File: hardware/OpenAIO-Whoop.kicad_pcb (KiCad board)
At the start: 6 copper layers, 30.3 x 30.3 mm, 248 parts, among them J1 U.FL, J10 M3, J13 M4, J2 +, J20 LED, J21 5V, J22 BZ-, J23 CAM, J24 5V, J25 GND, J26 VHD, J27 GND, J28 TX0, J29 RX0, J3 -, J31 USB, J32 CAM, J33 GND, J4 M1, J7 M2, Q26 AP1606, Q27 BC857BM, Q29 AGM210MAP, Q30 AGM210MAP, Q31 AGM210MAP, Q32 AGM210MAP, Q33 AGM210MAP, Q34 AGM210MAP, Q35 AGM210MAP, Q36 AGM210MAP, Q37 AGM210MAP, Q38 AGM210MAP, Q39 AGM210MAP, Q40 AGM210MAP, SW1 SKUBAAE010, U1 INA186A3, U10 RP2354A, U11 BMI270, U12 TPS7A2018, U13 PY25Q128HA-DFH-IR, U14 SN74LVC1G3157, U15 TLV7031, U16 ESP32-PICO-V3, U18 SX1281, U19 RTC6705, U2 TPS61022, U20 SE5004L, U21 LP5912-3.3, U22 TPS7A20285, U24 FXMAR2104UMX, U4 TLV75733, U6 EFM8BB51F16I, U7 EFM8BB51F16I, U8 EFM8BB51F16I, U9 EFM8BB51F16I, X1 12MHz, X3 52MHz TCXO, X4 8MHz 10pF

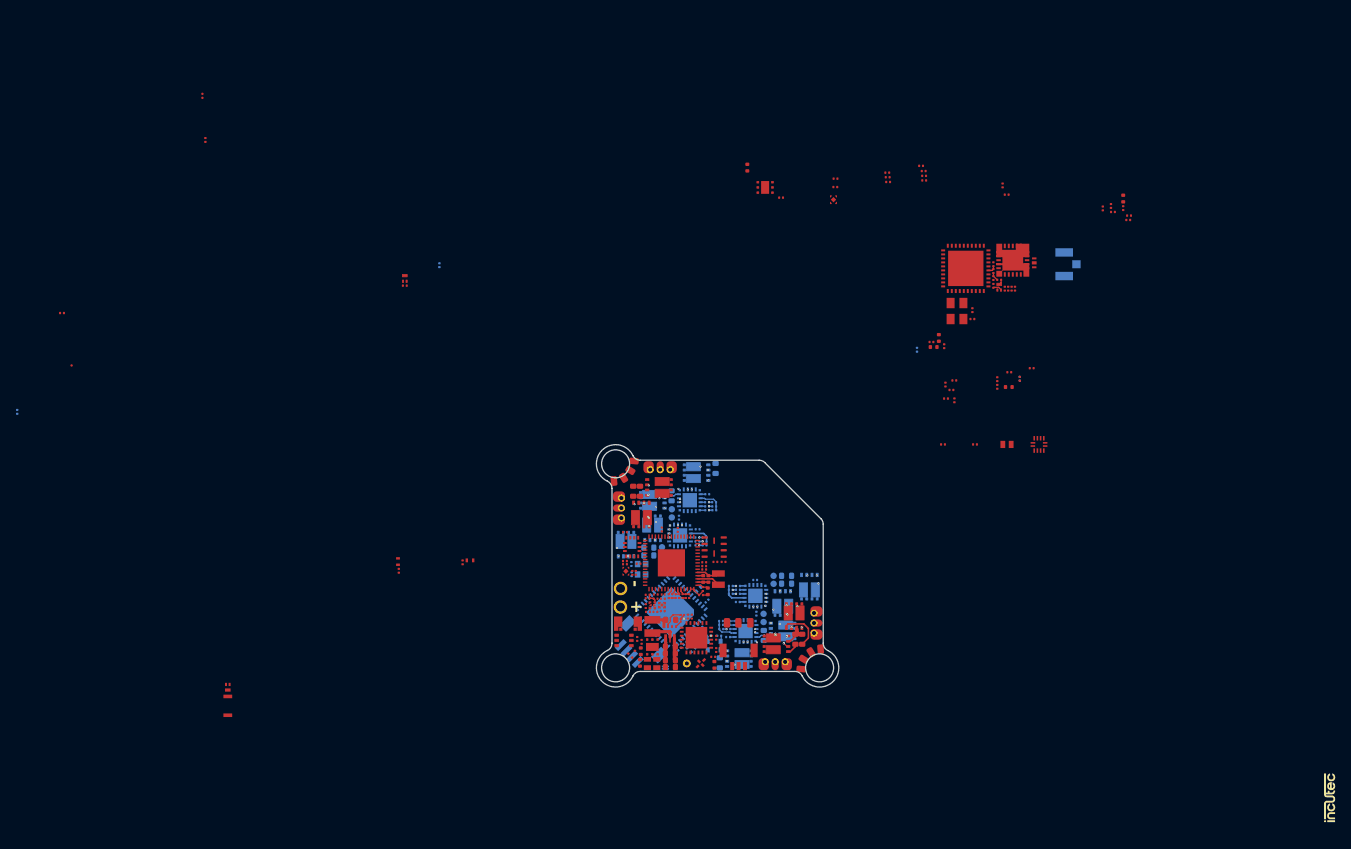
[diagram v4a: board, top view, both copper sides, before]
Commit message: Preserve owner ESC progress and allocate inner signal layers
Integrate the owner's retained placements and copper with the reviewed RP2354A mapping, restore both ESC bulk capacitors per channel, and carry the owner boot-testpoint deletion. Allocate In1/In4 for signals, In2 for continuous ground and In3 for power. Remove obsolete inner-layer routing restrictions and add native rule fixtures. This checkpoint precedes the new compact placement.

Validation: schematic parity zero; 28 GPIO mappings, 7 netlist checks and 32 rule fixtures pass. ERC has 12 existing warnings and no errors. The inherited board retains 269 DRC findings and 499 reported unconnected items. Layout is unfinished.
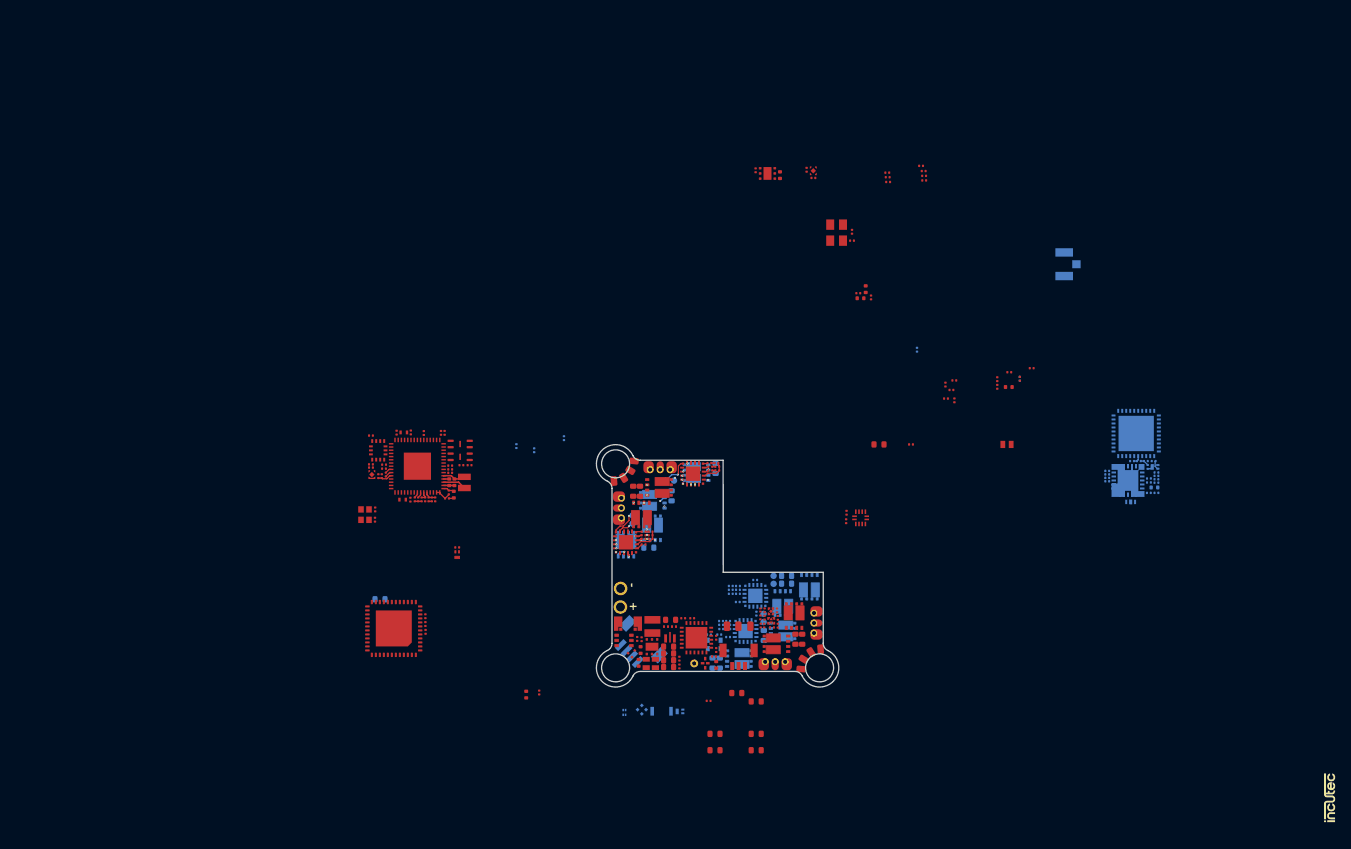
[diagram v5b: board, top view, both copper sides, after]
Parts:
- removed TP9: FCB, lib:TestPoint_Pad_D0.30mm_MicroVia_L
- added C22: 22uF, lib:C_0603_1608Metric_L, F.Cu at (118.0, 134.2)
- added C24: 22uF, lib:C_0603_1608Metric_L, F.Cu at (133.4, 98.0)
- added C28: 22uF, lib:C_0603_1608Metric_L, F.Cu at (112.9, 134.2)
- added C30: 22uF, lib:C_0603_1608Metric_L, F.Cu at (115.6, 129.1)
- added C34: 22uF, lib:C_0603_1608Metric_L, F.Cu at (118.0, 136.2)
- added C36: 22uF, lib:C_0603_1608Metric_L, B.Cu at (112.6, 125.3)
- added C40: 22uF, lib:C_0603_1608Metric_L, F.Cu at (112.9, 136.2)
- added C43: 22uF, lib:C_0603_1608Metric_L, F.Cu at (118.0, 130.2)
- C109, C110, C111, C112, C113, C114, C115, C116, C117, C118, C124, C125, D8, FL2, L3, Q27, R65, R66, R71, R72, R73, SW1, U19, U20: moved to B.Cu
- C42, C47, C70, C73, C76, C82, C83, C89, R26, R27, R28, R29, R30, R31, R32, R34, R35, R36, R37, R38, R39, R44, R56, U16, U8, U9, X1: moved to F.Cu
- moved C70 63.1 mm to (137.4, 98.0), turned to 0 degrees
- moved D8 56.6 mm to (108.5, 131.4), turned to 0 degrees
- moved SW1 54.2 mm to (106.2, 131.4), turned to 180 degrees
- moved R44 53.5 mm to (79.1, 96.6)
- moved TP13 53.0 mm to (71.7, 102.0), turned to 180 degrees
- moved TP12 52.2 mm to (71.7, 101.5), turned to 180 degrees
- moved C48 47.0 mm to (78.6, 96.6), turned to 90 degrees
- moved R49 44.5 mm to (71.5, 100.5)
- moved C117 43.0 mm to (168.1, 104.1), turned to 0 degrees
- moved R66 41.3 mm to (167.1, 104.1), turned to 0 degrees
- moved C118 36.3 mm to (167.8, 103.4), turned to 0 degrees
- moved X1 35.2 mm to (69.1, 106.8)
- moved Q26 35.1 mm to (80.7, 111.8), turned to 90 degrees
- moved C76 34.8 mm to (76.7, 121.4), turned to 90 degrees
- moved U16 34.8 mm to (72.7, 121.0), turned to 180 degrees
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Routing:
- net /ESC2/PHASE_A: track 13.5 -> 0.00 mm, vias 2 -> 0
- net /ESC3/PHASE_A: track 13.5 -> 2.01 mm
- net /ESC2/PHASE_B: track 10.7 -> 0.00 mm, vias 5 -> 0
- net /ESC1/PHASE_B: track 10.4 -> 0.00 mm, vias 3 -> 0
- net /ESC3/PHASE_B: track 10.7 -> 0.39 mm, vias 4 -> 0
- net GND: track 13.1 -> 3.24 mm, vias 1 -> 0
- net /ESC2/A_COM: track 9.78 -> 0.00 mm, vias 2 -> 0
- net /ESC4/PHASE_B: track 10.1 -> 0.41 mm, vias 2 -> 0
- net /ESC2/A_PWM: track 9.14 -> 0.00 mm, vias 2 -> 0
- net /ESC3/A_PWM: track 9.14 -> 0.39 mm, vias 2 -> 1
- net /ESC3/A_COM: track 9.78 -> 1.35 mm, vias 2 -> 1
- net /ESC1/PHASE_A: track 7.74 -> 0.00 mm, vias 2 -> 0
- net /ESC4/PHASE_A: track 7.73 -> 0.39 mm, vias 2 -> 0
- net /ESC1/PHASE_C: track 7.28 -> 0.00 mm, vias 2 -> 0
- net /ESC4/PHASE_C: track 7.28 -> 0.40 mm, vias 2 -> 0
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- added copper zone on In2.Cu, net GND
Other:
- outline, holes or cut-outs redrawn

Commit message: Build functional floorplan with checked power loops and RF reservations
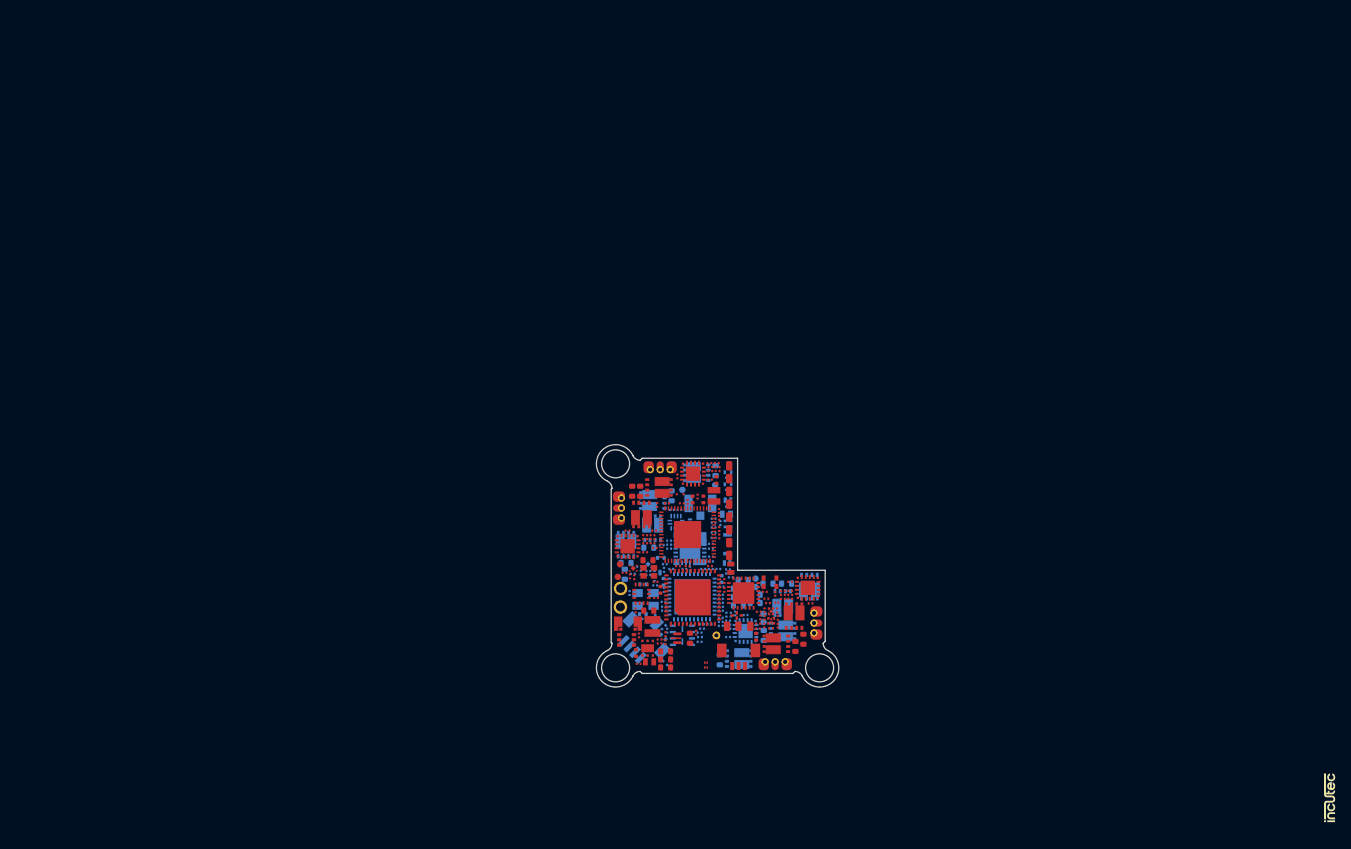
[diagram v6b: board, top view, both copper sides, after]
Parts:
- AE2, C25, C31, C37, C84, C85, R19, R20, R21, R22, R23, R24, R25, R33, TP5, TP6, U7, X3: moved to F.Cu
- C100, C101, C102, C103, C105, C106, C107, C108, C122, C123, C128, C135, C136, C143, C144, C22, C24, C28, C30, C34, C43, C59, C60, C65, C73, C83, C91, C94, C95, C98, D10, D5, D6, D7, Q26, R45, R46, R47, R48, R50, R56, R58, R59, R60, R61, R62, R63, R64, R68, R80, R81, R82, R85, R86, R89, R90, U13, U21, U22, U24, X4: moved to B.Cu
- moved R71 66.4 mm to (102.6, 114.2)
- moved C124 65.5 mm to (103.6, 114.0), turned to 90 degrees
- moved R72 64.7 mm to (104.5, 114.3)
- moved R73 64.6 mm to (104.5, 113.8)
- moved C125 64.2 mm to (105.3, 114.8), turned to -90 degrees
- moved Q27 63.6 mm to (105.7, 114.0), turned to 180 degrees
- moved R90 63.5 mm to (111.2, 120.5), turned to 0 degrees
- moved C136 63.0 mm to (111.2, 121.0), turned to 0 degrees
- moved C118 62.3 mm to (106.1, 112.2), turned to 180 degrees
- moved C117 62.2 mm to (106.2, 110.6), turned to 180 degrees
- moved R65 61.8 mm to (106.5, 113.7)
- moved C109 61.5 mm to (106.6, 113.0), turned to 180 degrees
- moved R66 60.3 mm to (107.1, 110.0), turned to 180 degrees
- moved C122 59.7 mm to (104.0, 119.8), turned to 180 degrees
- moved U19 59.2 mm to (110.0, 117.0), turned to 180 degrees
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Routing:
- net /ESC3/B_PWM: track 12.2 -> 0.00 mm, vias 2 -> 0
- net /ESC3/B_COM: track 11.7 -> 0.00 mm, vias 2 -> 0
- net /ESC4/B_PWM: track 7.20 -> 0.00 mm, vias 2 -> 0
- net /ESC4/A_PWM: track 7.13 -> 0.00 mm, vias 2 -> 0
- net +3.3V: track 6.11 -> 0.00 mm
- net /ESC4/B_COM: track 5.18 -> 0.00 mm, vias 2 -> 0
- net /ESC3/C_PWM: track 5.07 -> 0.00 mm, vias 2 -> 0
- net /ESC4/A_COM: track 4.46 -> 0.00 mm, vias 2 -> 0
- net /ESC4/C_PWM: track 4.31 -> 0.00 mm, vias 2 -> 0
- net +1.1V: track 3.64 -> 0.00 mm
- net /ESC4/C2D: track 3.62 -> 0.00 mm, vias 1 -> 0
- net /ESC3/C_COM: track 3.57 -> 0.00 mm, vias 2 -> 0
- net /ESC4/C_COM: track 3.51 -> 0.00 mm, vias 2 -> 0
- net GND: track 3.24 -> 0.00 mm
- net /ESC4/NEUTRAL: track 3.22 -> 0.00 mm
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- removed copper zone on In3.Cu, net +BATT
- removed copper zone on In1.Cu, net GND
- removed copper zone on In2.Cu, net GND
- removed copper zone on In4.Cu, net GND
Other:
- outline, holes or cut-outs redrawn
- board text removed: "+"
- board text removed: "-"
- board text removed: "M1"
- board text removed: "M2"
- board text removed: "M3"
- board text removed: "M4"

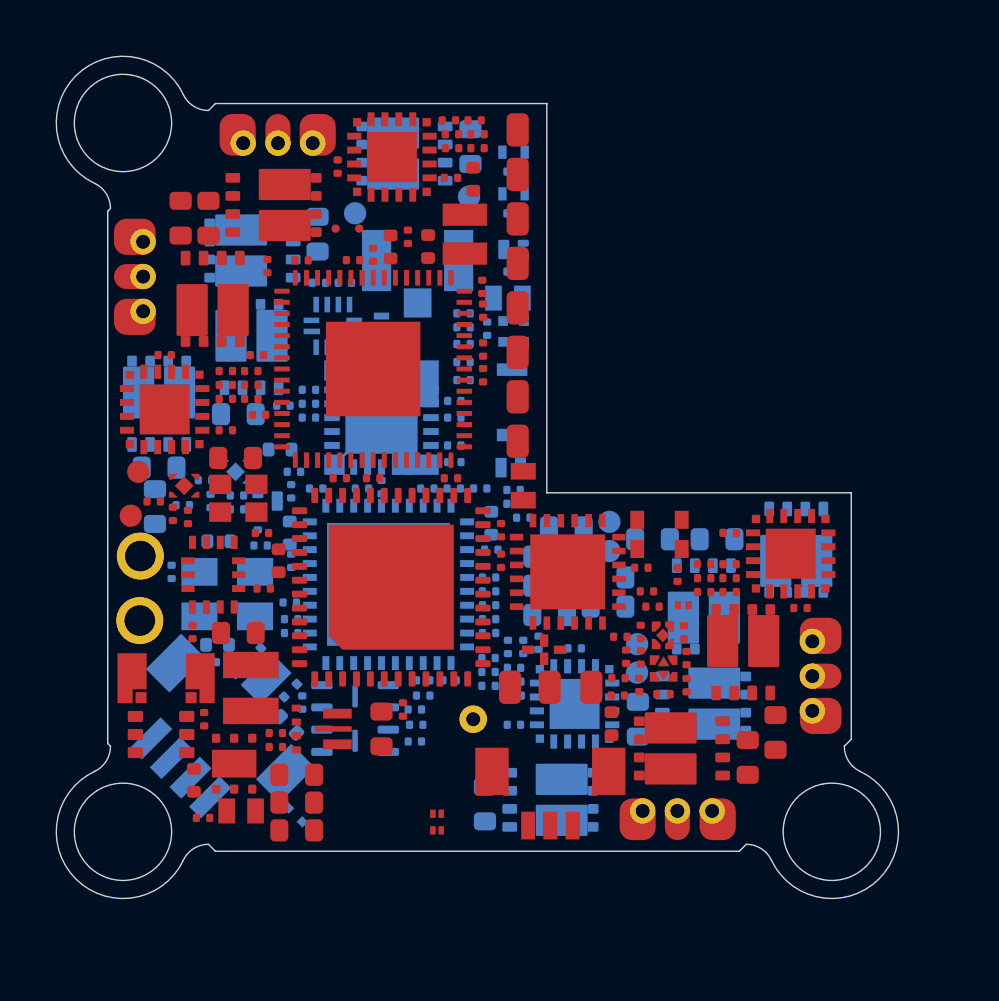
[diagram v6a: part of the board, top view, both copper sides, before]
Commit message: Route local ESC and VTX connections and compact Wi-Fi antenna layout
Add the fitted series link and two optional matching lands. Replace the large antenna reservation with a documented compact prototype window and shorten its feed. Preserve motor connector and half-bridge placement.

Integrate checked ESC gate/BEMF, boost and VTX copper, with filled and capped staggered HDI vias and local ground references. Remove stale layout guidance and refresh schematic exports.

137 connection groups pass. Native DRC has no copper errors or schematic parity findings; 138 existing warnings and 468 open connections remain. Routing and RF performance validation are incomplete.
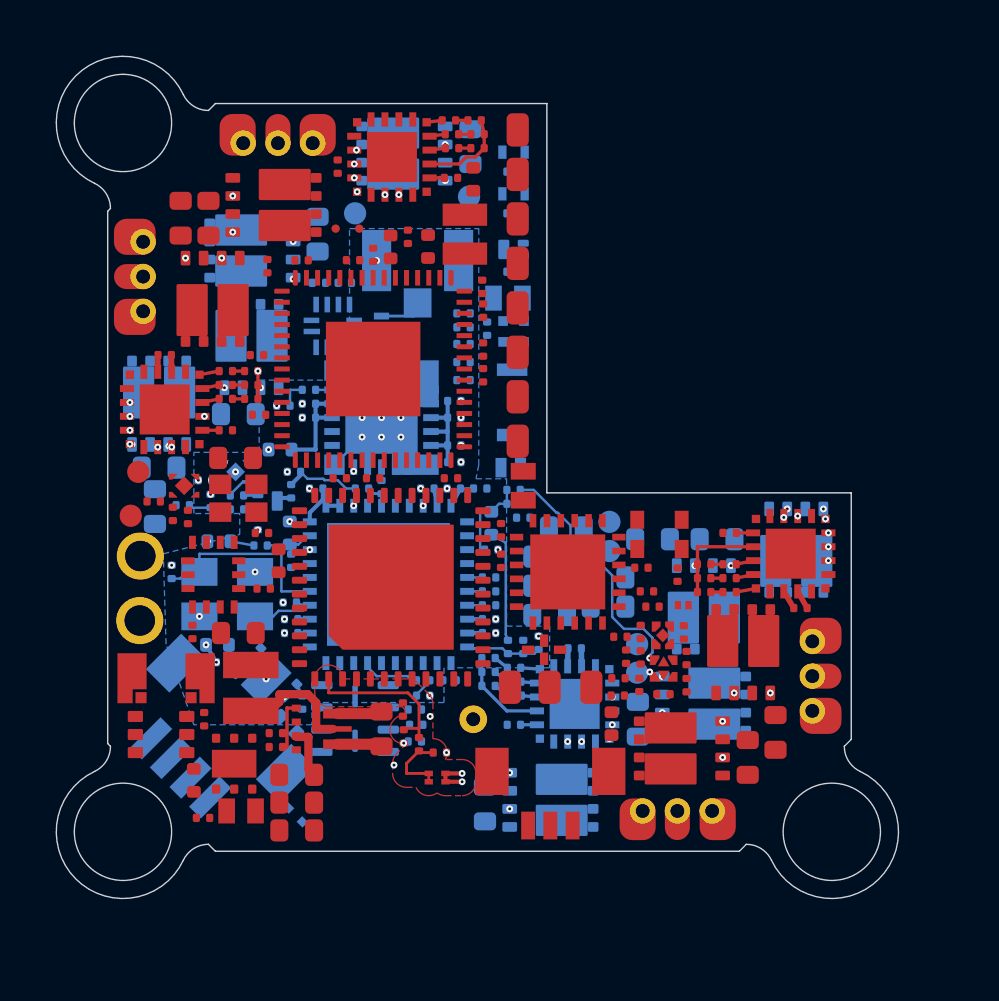
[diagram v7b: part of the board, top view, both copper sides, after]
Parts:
- added C132: DNP, lib:C_0201_0603Metric_L, F.Cu at (111.8, 123.1)
- added C133: DNP, lib:C_0201_0603Metric_L, F.Cu at (110.5, 122.5)
- added R88: 0R, lib:R_0201_0603Metric_L, F.Cu at (111.1, 122.8)
- moved AE2 1.60 mm to (111.8, 124.0), turned to -90 degrees
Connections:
- AE2 pad 1: /RX/RF_WIFI -> /RX/RF_WIFI_ANT
- AE2 pad 4: /RX/RF_WIFI -> /RX/RF_WIFI_ANT
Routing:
- net /ESC2/C_COM: track 0.00 -> 16.3 mm, vias 0 -> 3
- net /ESC3/B_PWM: track 0.00 -> 13.8 mm, vias 0 -> 2
- net /ESC2/C_PWM: track 0.00 -> 13.8 mm, vias 0 -> 3
- net /VIDEO_OUT: track 0.00 -> 9.64 mm, vias 0 -> 3
- net +BATT: track 0.00 -> 9.63 mm
- net /ESC2/B_PWM: track 0.00 -> 7.62 mm, vias 0 -> 2
- net /ESC3/B_COM: track 0.00 -> 7.31 mm, vias 0 -> 2
- net /ESC4/B_PWM: track 0.00 -> 7.20 mm, vias 0 -> 2
- net /ESC4/A_PWM: track 0.00 -> 7.08 mm, vias 0 -> 3
- net /VTX/U19_XTAL2: track 0.00 -> 7.07 mm
- net /ESC2/B_COM: track 0.00 -> 6.63 mm, vias 0 -> 2
- net +3.3V_VTX: track 0.00 -> 6.60 mm
- net /ESC1/B_PWM: track 0.00 -> 5.91 mm, vias 0 -> 3
- net /VTX/PA_VREF: track 0.00 -> 5.78 mm, vias 0 -> 2
- net GND: track 0.00 -> 5.77 mm, vias 0 -> 83
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- added copper zone on B.Cu, net GND
- added copper zone on F.Cu, net GND
- added copper zone on In1.Cu, net GND
- added copper zone on In2.Cu, net GND
- added copper zone on In4.Cu, net GND
